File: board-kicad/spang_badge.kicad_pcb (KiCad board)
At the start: 2 copper layers, 37.5 x 43.5 mm, 3 parts

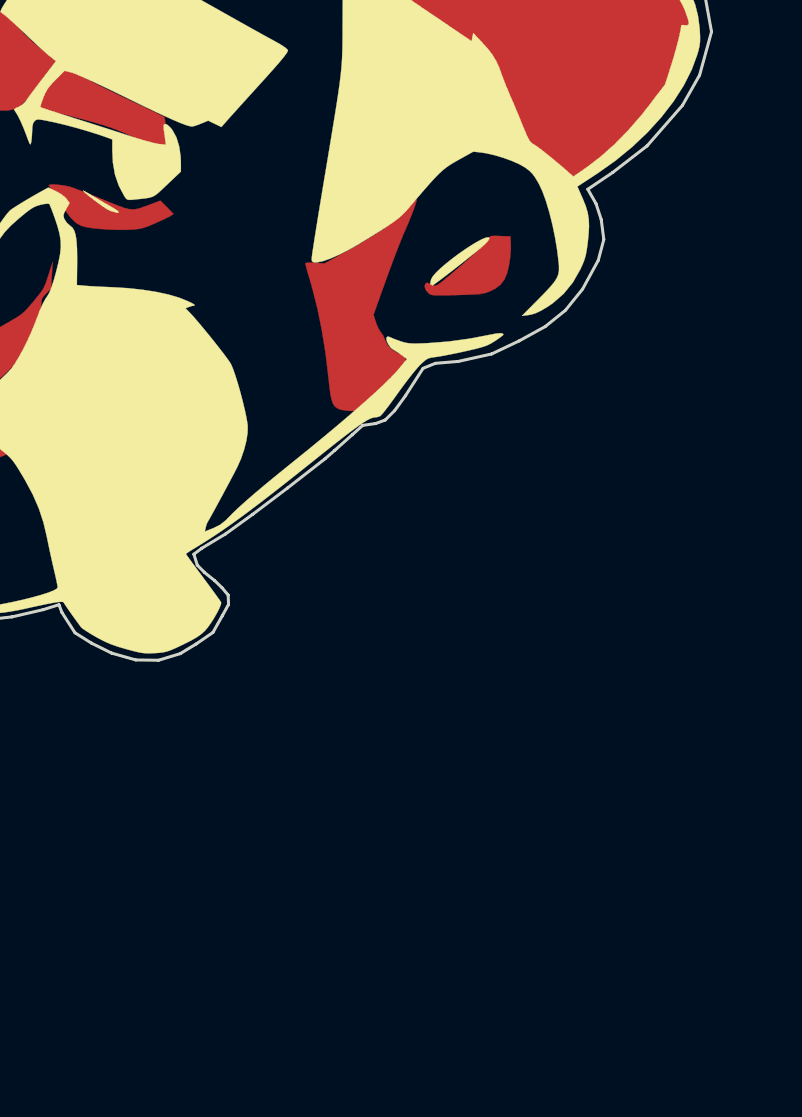
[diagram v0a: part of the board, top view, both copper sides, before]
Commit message: fixed the Shroom design so the mouth isn't covered by silkscreen
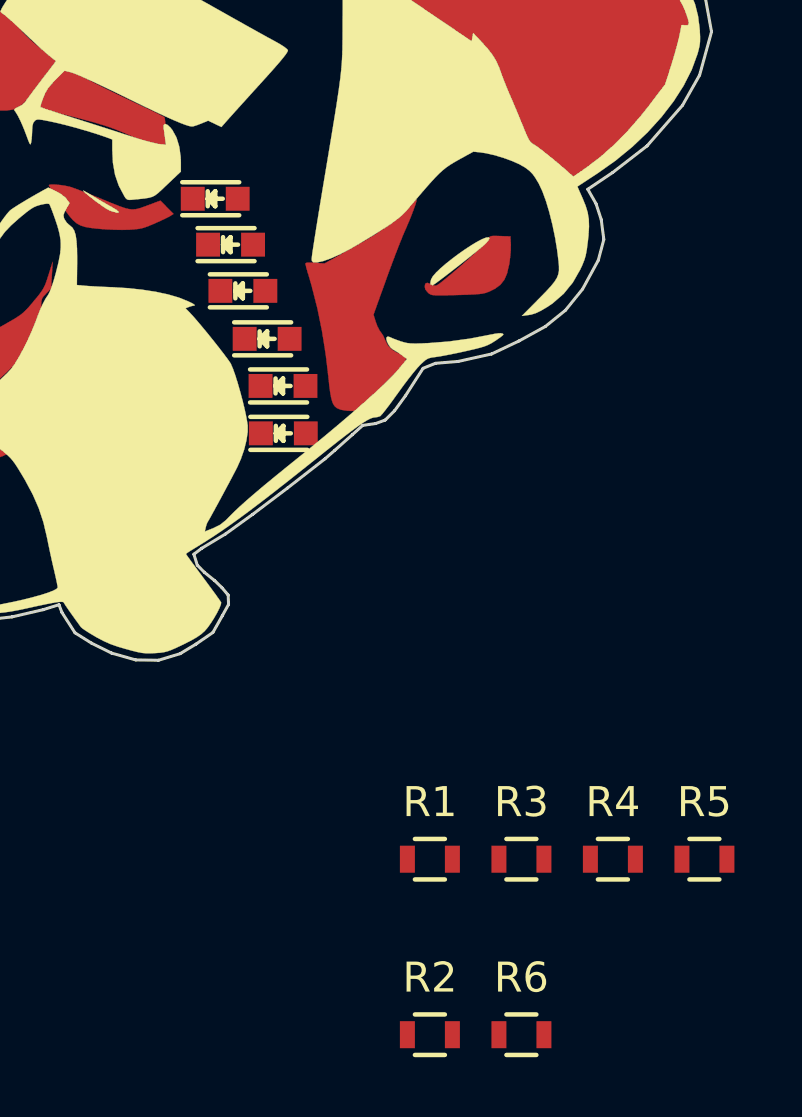
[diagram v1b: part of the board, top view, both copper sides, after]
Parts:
- removed the G*** at (128.8, 102.6) (x3)
- added D1: LED, LEDs:LED_0603, F.Cu at (129.4, 108.7)
- added D2: LED, LEDs:LED_0603, F.Cu at (129.9, 110.2)
- added D3: LED, LEDs:LED_0603, F.Cu at (130.3, 111.8)
- added D4: LED, LEDs:LED_0603, F.Cu at (131.2, 113.4)
- added D5: LED, LEDs:LED_0603, F.Cu at (131.7, 115.0)
- added D6: LED, LEDs:LED_0603, F.Cu at (131.7, 116.5)
- added G*** (x3): LOGO, LOGO, F.Cu at (128.8, 102.6)
- added R1: R, Resistors_SMD:R_0603, F.Cu at (136.6, 130.7)
- added R2: R, Resistors_SMD:R_0603, F.Cu at (136.6, 136.6)
- added R3: R, Resistors_SMD:R_0603, F.Cu at (139.6, 130.7)
- added R4: R, Resistors_SMD:R_0603, F.Cu at (142.7, 130.7)
- added R5: R, Resistors_SMD:R_0603, F.Cu at (145.7, 130.7)
- added R6: R, Resistors_SMD:R_0603, F.Cu at (139.6, 136.6)

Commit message: cleaned up sponge
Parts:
- removed D1, D2, D3, D4, D5, D6: LED, LEDs:LED_0603
- removed the G*** at (128.8, 102.6) (x3)
- removed R1, R2, R3, R4, R5, R6: R, Resistors_SMD:R_0603
- added G*** (x3): LOGO, LOGO, F.Cu at (90.2, 73.2)
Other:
- outline, holes or cut-outs redrawn

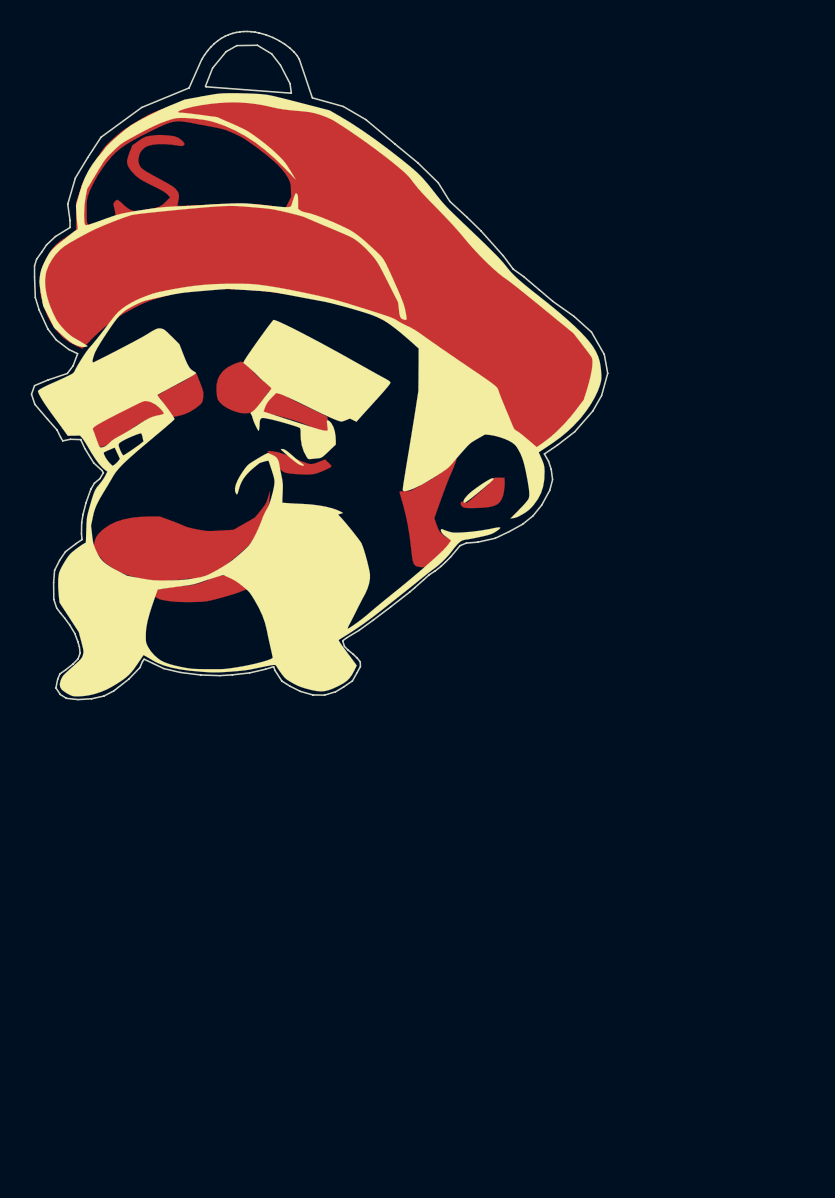
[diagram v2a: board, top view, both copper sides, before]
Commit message: starting LED placement
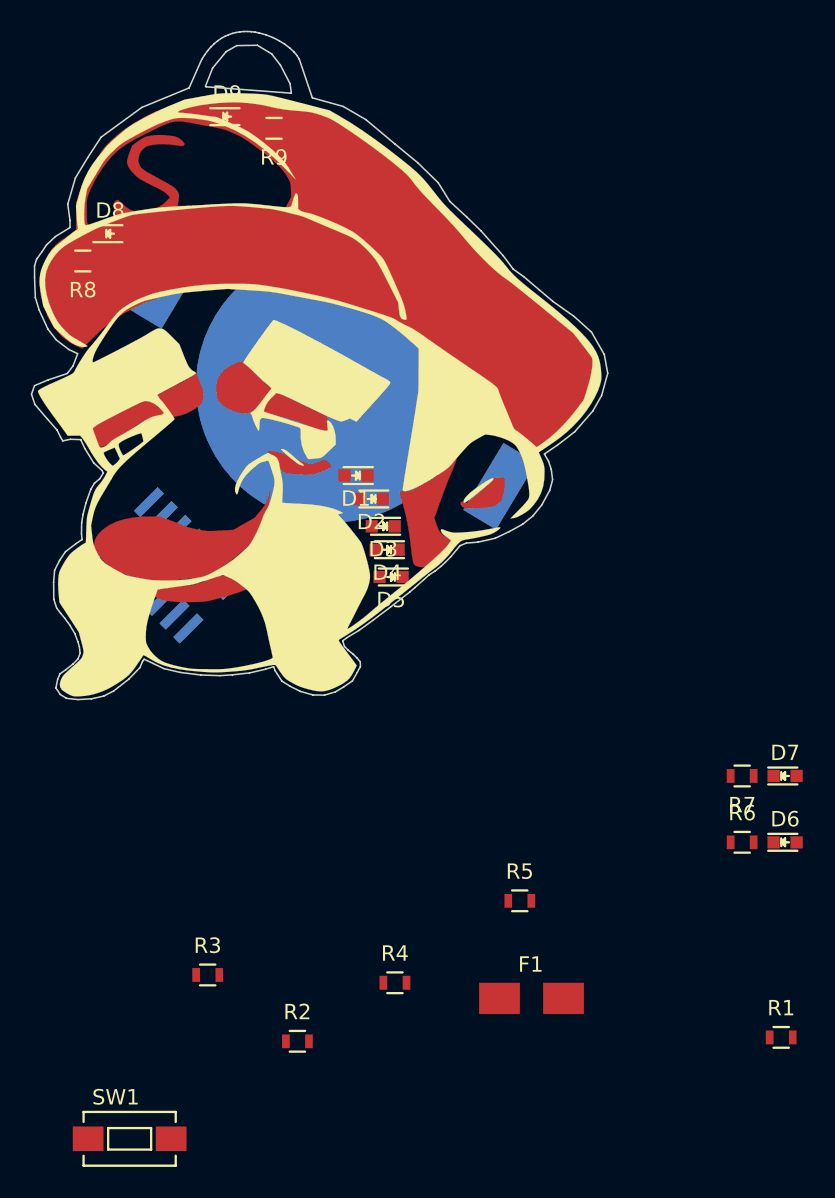
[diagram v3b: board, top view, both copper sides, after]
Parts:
- removed the G*** at (90.2, 73.2) (x3)
- added BT1: Battery_Cell, spang_badge:COINCELL_20MM, B.Cu at (62.0, 47.0)
- added D1: LED, LEDs:LED_0603, F.Cu at (63.5, 52.8)
- added D2: LED, LEDs:LED_0603, F.Cu at (64.5, 54.4)
- added D3: LED, LEDs:LED_0603, F.Cu at (65.3, 56.1)
- added D4: LED, LEDs:LED_0603, F.Cu at (65.5, 57.7)
- added D5: LED, LEDs:LED_0603, F.Cu at (65.8, 59.4)
- added D6: LED, LEDs:LED_0603, F.Cu at (91.4, 76.7)
- added D7: LED, LEDs:LED_0603, F.Cu at (91.4, 72.4)
- added D8: LED, LEDs:LED_0603, F.Cu at (47.5, 37.1)
- added D9: LED, LEDs:LED_0603, F.Cu at (55.1, 29.5)
- added F1: Fuse, Fuse_Holders_and_Fuses:Fuse_SMD1206_HandSoldering, F.Cu at (74.9, 86.9)
- added G*** (x3): LOGO, LOGO, F.Cu at (90.2, 73.2)
- added IC1: ATTINY20-X, spang_badge:ATTINY20_SOIC-14, B.Cu at (51.3, 58.7)
- added R1: R, Resistors_SMD:R_0603, F.Cu at (91.2, 89.4)
- added R2: R, Resistors_SMD:R_0603, F.Cu at (59.7, 89.7)
- added R3: R, Resistors_SMD:R_0603, F.Cu at (53.8, 85.3)
- added R4: R, Resistors_SMD:R_0603, F.Cu at (66.0, 85.9)
- added R5: R, Resistors_SMD:R_0603, F.Cu at (74.2, 80.5)
- added R6: R, Resistors_SMD:R_0603, F.Cu at (88.6, 76.7)
- added R7: R, Resistors_SMD:R_0603, F.Cu at (88.6, 72.4)
- added R8: R, Resistors_SMD:R_0603, F.Cu at (45.7, 38.9)
- added R9: R, Resistors_SMD:R_0603, F.Cu at (58.2, 30.2)
- added SW1: SW_DPST, Buttons_Switches_SMD:SW_SPST_EVQPE1, F.Cu at (48.8, 96.0)

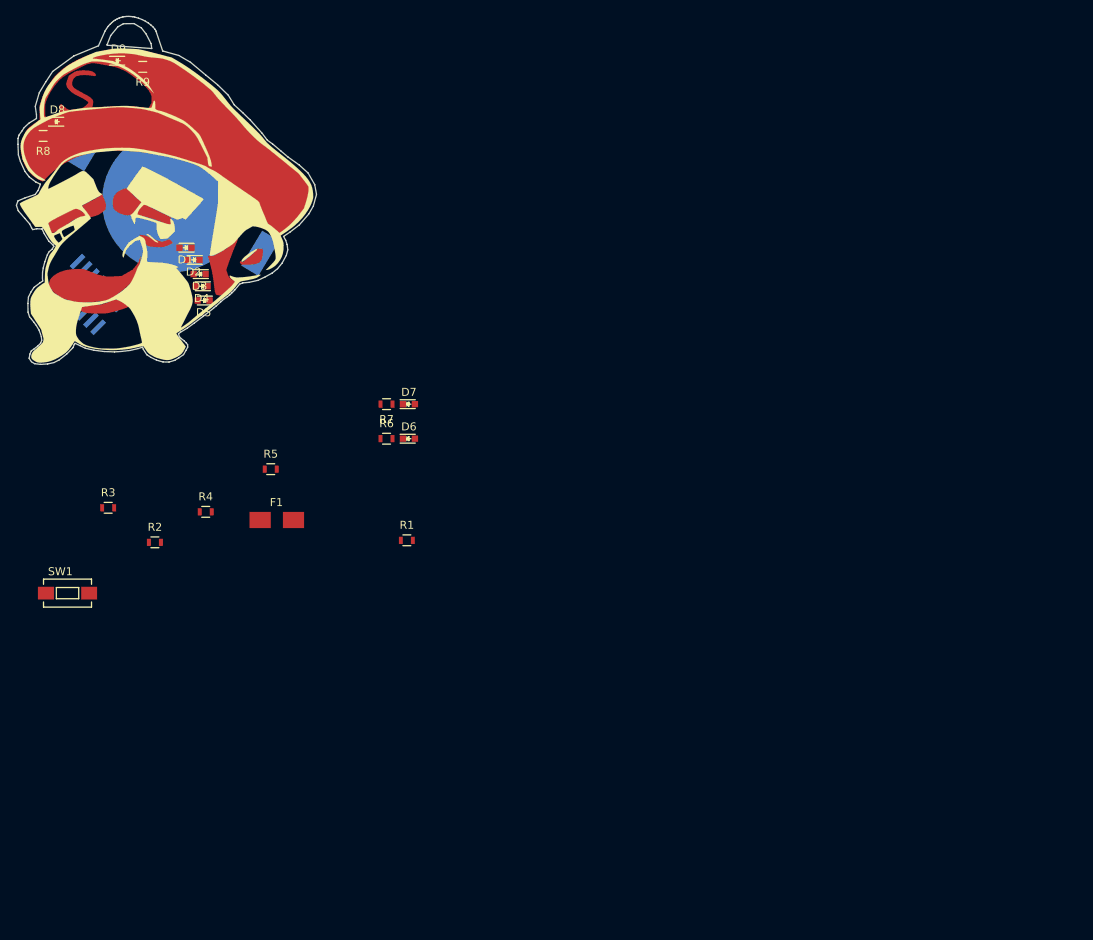
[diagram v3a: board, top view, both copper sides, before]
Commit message: routing sponge. Need to figure out how to rename polygons to GND
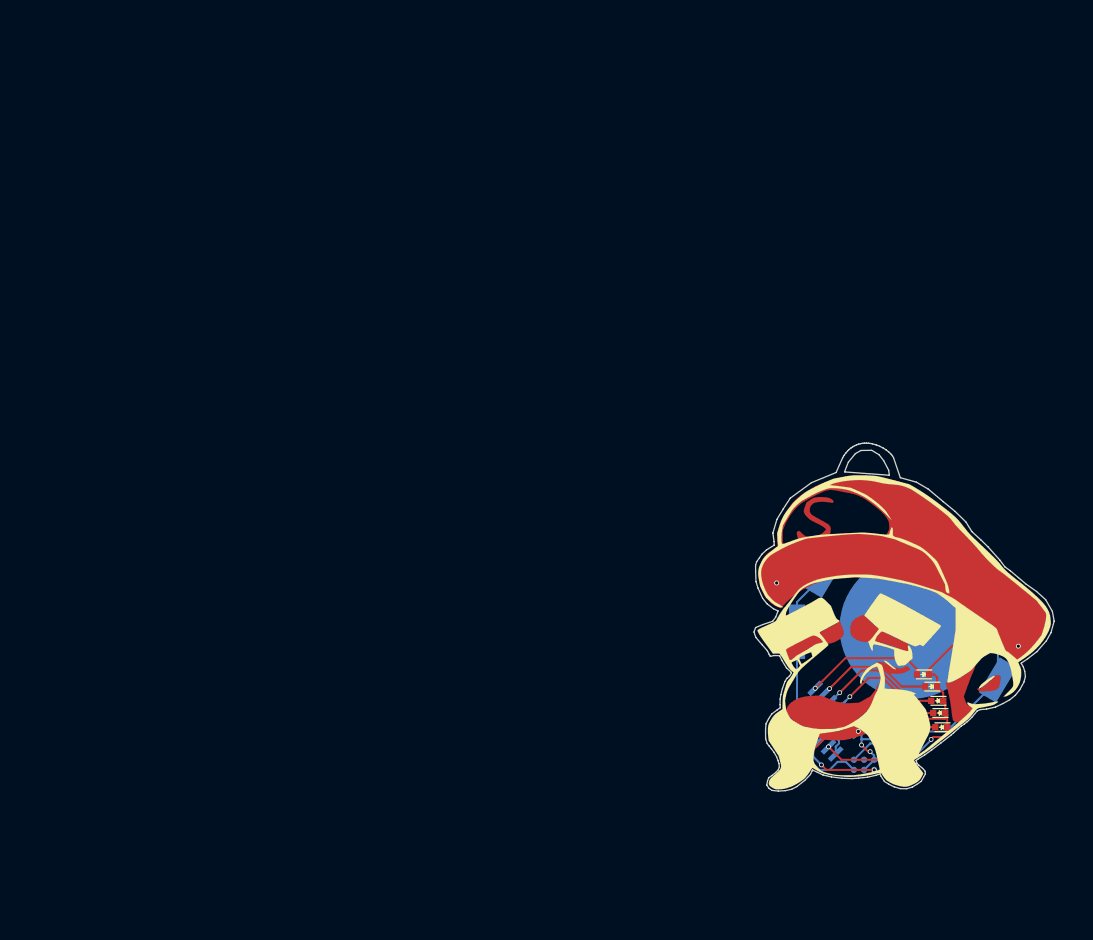
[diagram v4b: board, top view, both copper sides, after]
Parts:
- removed D6, D9: LED, LEDs:LED_0603
- removed the G*** at (90.2, 73.2) (x3)
- removed R3, R4, R5, R6, R7, R8, R9: R, Resistors_SMD:R_0603
- added G*** (x3): LOGO, LOGO, F.Cu at (182.4, 126.5)
- added J1: CONN-TAGCONNECT-TC2050, spang_badge:TC2050_IDC, B.Cu at (149.6, 117.5)
- added Q1: Q_NMOS_GSD, TO_SOT_Packages_SMD:SOT-23, B.Cu at (151.6, 113.3)
- D7, D8, F1, R1, R2: moved to B.Cu
- SW1: value SW_DPST -> SW_SPST; footprint Buttons_Switches_SMD:SW_SPST_EVQPE1 -> Buttons_Switches_SMD:SW_SPST_B3U-3000P; moved to B.Cu
- moved D8 109.5 mm to (143.5, 89.7), turned to 9 degrees
- moved D4 106.5 mm to (157.7, 111.0)
- moved BT1 106.5 mm to (154.2, 100.3)
- moved D1 106.5 mm to (155.7, 106.2)
- moved D5 106.5 mm to (158.0, 112.8)
- moved IC1 106.5 mm to (143.5, 112.0)
- moved D2 106.5 mm to (156.7, 107.7)
- moved D3 106.5 mm to (157.5, 109.5)
- moved SW1 92.1 mm to (138.9, 114.8), turned to 315 degrees
- moved R2 80.5 mm to (140.2, 90.7), turned to 180 degrees
- moved R1 78.0 mm to (168.1, 102.1), turned to 225 degrees
- moved F1 66.5 mm to (140.0, 100.8), turned to 90 degrees
- moved D7 56.6 mm to (147.1, 82.8), turned to 165 degrees
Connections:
- net /BACKLIGHT renamed Net-(IC1-Pad6)
- D1 pad 1: Net-(D1-Pad1) -> GND
- D2 pad 1: Net-(D2-Pad1) -> GND
- D3 pad 1: Net-(D3-Pad1) -> GND
- D4 pad 1: Net-(D4-Pad1) -> GND
- D5 pad 1: Net-(D5-Pad1) -> GND
- IC1 pad 2: Net-(IC1-Pad2) -> /TCK
- IC1 pad 3: Net-(IC1-Pad3) -> /TDI
- IC1 pad 4: Net-(IC1-Pad4) -> /nRST
- R1 pad 1: Net-(D1-Pad1) -> Net-(D7-Pad1)
- R2 pad 1: Net-(D2-Pad1) -> Net-(D8-Pad1)
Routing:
- net +BATT: track 0.00 -> 109.3 mm
- net GND: track 0.00 -> 59.1 mm, vias 0 -> 6
- net Net-(D7-Pad1): track 0.00 -> 29.2 mm
- net Net-(D4-Pad2): track 0.00 -> 17.1 mm, vias 0 -> 1
- net Net-(D3-Pad2): track 0.00 -> 16.6 mm, vias 0 -> 1
- net Net-(F1-Pad1): track 0.00 -> 15.5 mm
- net Net-(D1-Pad2): track 0.00 -> 15.5 mm, vias 0 -> 1
- net /nRST: track 0.00 -> 15.3 mm
- net Net-(D2-Pad2): track 0.00 -> 14.2 mm, vias 0 -> 1
- net Net-(BT1-Pad2): track 0.00 -> 13.6 mm
- net Net-(D5-Pad2): track 0.00 -> 12.7 mm, vias 0 -> 1
- net /TDI: track 0.00 -> 10.9 mm, vias 0 -> 2
- net /TCK: track 0.00 -> 7.65 mm, vias 0 -> 2
- net (no net): track 0.00 -> 5.65 mm, vias 0 -> 1
- net Net-(IC1-Pad7): track 0.00 -> 3.56 mm
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
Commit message: need to run DRC
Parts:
- removed the G*** at (182.4, 126.5) (x3)
- added G*** (x3): LOGO, LOGO, F.Cu at (182.4, 126.5)
- SW1: footprint Buttons_Switches_SMD:SW_SPST_B3U-3000P -> spang_badge:EVQ-P7B01P
- moved SW1 0.76 mm to (138.9, 115.6), turned to 120 degrees
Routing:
- net GND: track 59.1 -> 108.4 mm, vias 6 -> 7
- net /nRST: track 15.3 -> 10.8 mm
- net (no net): track 5.65 -> 1.51 mm, vias 1 -> 0
- net Net-(IC1-Pad7): track 3.56 -> 6.89 mm

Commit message: final touches on shroom badge
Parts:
- removed the G*** at (182.4, 126.5) (x3)
- added G***: LOGO, LOGO, B.Cu at (135.2, 86.2)
- added G*** (x3): LOGO, LOGO, F.Cu at (182.4, 126.5)
- moved D7 4.33 mm to (150.7, 85.1), turned to 320 degrees
- moved D8 0.28 mm to (143.4, 89.4)
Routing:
- net +BATT: track 109.3 -> 77.9 mm
- net Net-(D7-Pad1): track 29.2 -> 26.2 mm
- net Net-(D2-Pad2): track 14.2 -> 15.4 mm
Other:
- net class Default: clearance 0.2 -> 0.1
- rule trace_clearance: 0.2 -> 0.1
